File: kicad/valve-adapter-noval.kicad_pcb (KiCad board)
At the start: 2 copper layers, 28 x 34 mm, 3 parts, among them J1 Conn_01x09, U1 ECC83

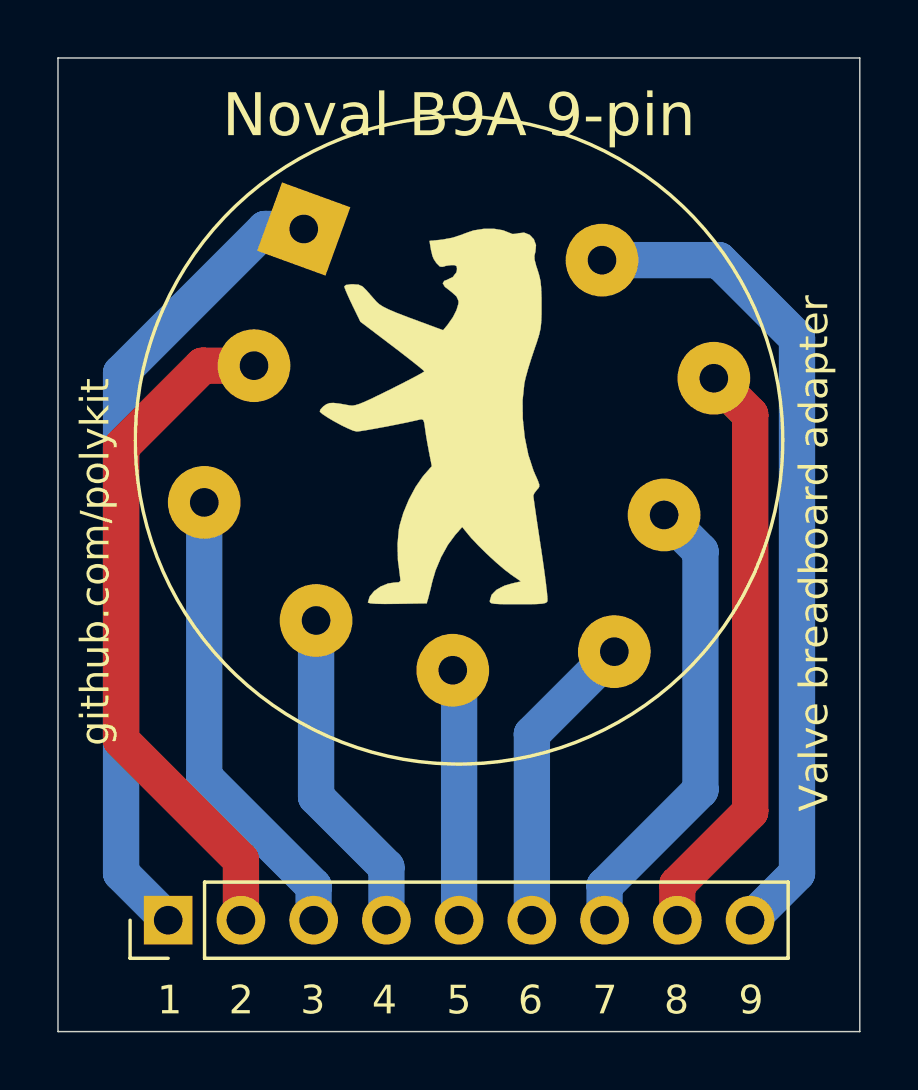
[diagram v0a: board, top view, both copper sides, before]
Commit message: Changed valve footprint
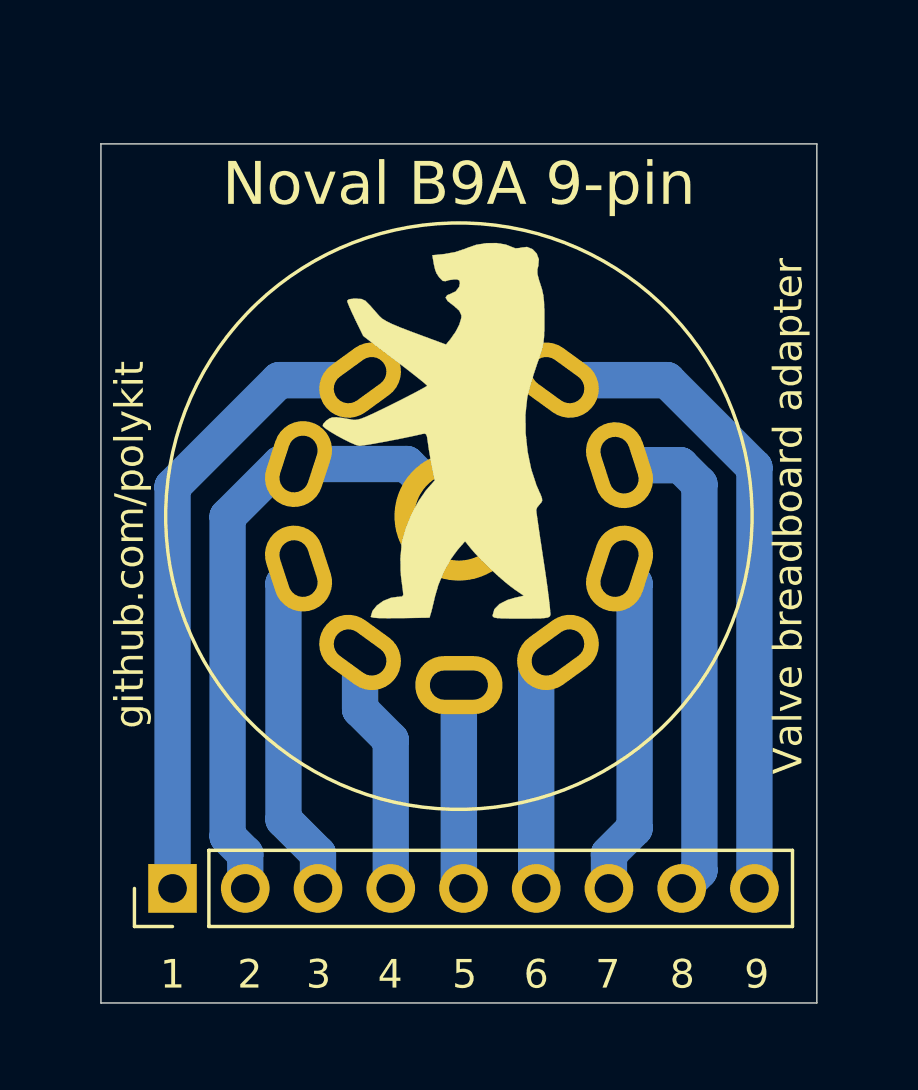
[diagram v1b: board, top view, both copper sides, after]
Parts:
- U1: footprint Valve:Valve_Noval_P -> Valve:Valve_ECC-83-2
- moved U1 5.63 mm to (159.6, 97.2), turned to 180 degrees
- moved J1 1.12 mm to (153.0, 115.0)
- moved G*** 0.51 mm to (162.4, 99.1)
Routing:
- net Net-(J1-Pad1): track 28.3 -> 22.1 mm
- net Net-(J1-Pad9): track 28.9 -> 22.8 mm
- net Net-(J1-Pad7): track 16.1 -> 11.8 mm
- net Net-(J1-Pad3): track 16.2 -> 11.9 mm
- net Net-(J1-Pad8): track 20.5 -> 17.4 mm
- net Net-(J1-Pad4): track 11.5 -> 8.68 mm
- net Net-(J1-Pad6): track 10.6 -> 8.55 mm
- net Net-(J1-Pad5): track 8.82 -> 7.17 mm
- net Net-(J1-Pad2): track 24.1 -> 22.8 mm
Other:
- board size 28 x 34 mm -> 25 x 30 mm
- net class Default: clearance 1 -> 0.5
- rule trace_clearance: 1 -> 0.5
